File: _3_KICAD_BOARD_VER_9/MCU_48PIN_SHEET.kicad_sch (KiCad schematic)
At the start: 16 parts, among them U2 dsPIC33AK512MPS505T-I/PT, Y1 ABMM-25.000MHZ-B2-T

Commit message: feat : dim only project done
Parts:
- renumbered C18 to C10, C19 to C11, C20 to C12, C21 to C13, C22 to C14, C23 to C15, C24 to C16, C25 to C17, C13 to C5, C14 to C6, C15 to C7, C16 to C8, C17 to C9

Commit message: feat : dim board base board 작업시작
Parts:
- C10, C12, C14, C15, C16, C5, C6, C8: LCSC Part # (none) -> C14663
- C11: LCSC Part # (none) -> C19702
- C13, C17: LCSC Part # (none) -> C107040
- C7: LCSC Part # (none) -> C140782
- C9: LCSC Part # (none) -> C5199872
- L1: LCSC Part # (none) -> C86083
- Y1: LCSC Part # (none) -> C596927
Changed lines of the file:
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@@
+			)
+		)
+		(property "LCSC Part #" "C140782"
+			(at 35.56 41.91 0)
+			(effects
+				(font
+					(size 1.27 1.27)
+				)
+				(hide yes)
 			)
 		)
@@
 			)
 		)
+		(property "LCSC Part #" "C596927"
+			(at 232.41 143.51 0)
+			(effects
+				(font
+					(size 1.27 1.27)
+				)
+				(hide yes)
+			)
+		)
 		(pin "4"
 		)
@@
 			)
 		)
+		(property "LCSC Part #" "C14663"
+			(at 38.1 78.74 0)
+			(effects
+				(font
+					(size 1.27 1.27)
+				)
+				(hide yes)
+			)
+		)
 		(pin "2"
 		)
@@
 			)
 		)
+		(property "LCSC Part #" "C107040"
+			(at 246.38 146.05 0)
+			(effects
+				(font
+					(size 1.27 1.27)
+				)
+				(hide yes)
+			)
+		)
 		(pin "1"
 		)
@@
 			)
 		)
+		(property "LCSC Part #" "C14663"
+			(at 160.02 33.02 0)
+			(effects
+				(font
+					(size 1.27 1.27)
+				)
+				(hide yes)
+			)
+		)
 		(pin "2"
 		)
@@
 			)
 		)
+		(property "LCSC Part #" "C14663"
+			(at 224.79 95.25 0)
+			(effects
+				(font
+					(size 1.27 1.27)
+				)
+				(hide yes)
+			)
+		)
 		(pin "2"
 		)
@@
 			)
 		)
+		(property "LCSC Part #" "C107040"
+			(at 214.63 146.05 0)
+			(effects
+				(font
+					(size 1.27 1.27)
+				)
+				(hide yes)
+			)
+		)
 		(pin "1"
 		)
@@
 			)
 		)
+		(property "LCSC Part #" "C14663"
+			(at 227.33 69.85 0)
+			(effects
+				(font
+					(size 1.27 1.27)
+				)
+				(hide yes)
+			)
+		)
 		(pin "2"
 		)
@@
 			)
 		)
+		(property "LCSC Part #" "C14663"
+			(at 207.01 33.02 0)
+			(effects
+				(font
+					(size 1.27 1.27)
+				)
+				(hide yes)
+			)
+		)
 		(pin "2"
 		)
@@
 			)
 		)
+		(property "LCSC Part #" ""
+			(at 80.01 62.23 0)
+			(effects
+				(font
+					(size 1.27 1.27)
+				)
+				(hide yes)
+			)
+		)
 		(pin "11"
 		)
@@
 			)
 		)
+		(property "LCSC Part #" "C5199872"
+			(at 45.72 41.91 0)
+			(effects
+				(font
+					(size 1.27 1.27)
+				)
+				(hide yes)
+			)
+		)
 		(pin "2"
 		)
@@
 			)
 		)
+		(property "LCSC Part #" "C86083"
+			(at 187.96 30.48 90)
+			(effects
+				(font
+					(size 1.27 1.27)
+				)
+				(hide yes)
+			)
+		)
 		(pin "2"
 		)
@@
 			)
 		)
+		(property "LCSC Part #" "C19702"
+			(at 195.58 33.02 0)
+			(effects
+				(font
+					(size 1.27 1.27)
+				)
+				(hide yes)
+			)
+		)
 		(pin "2"
 		)
@@
 			)
 		)
+		(property "LCSC Part #" "C14663"
+			(at 232.41 115.57 0)
+			(effects
+				(font
+					(size 1.27 1.27)
+				)
+				(hide yes)
+			)
+		)
 		(pin "2"
 		)
@@
 			)
 		)
+		(property "LCSC Part #" "C14663"
+			(at 34.29 100.33 0)
+			(effects
+				(font
+					(size 1.27 1.27)
+				)
+				(hide yes)
+			)
+		)
 		(pin "2"
 		)
@@
 			(at 29.21 113.03 0)
 			(effects
+				(font
+					(size 1.27 1.27)
+				)
+				(hide yes)
+			)
+		)
+		(property "LCSC Part #" "C14663"
+			(at 29.21 113.03 0)
+			(effects

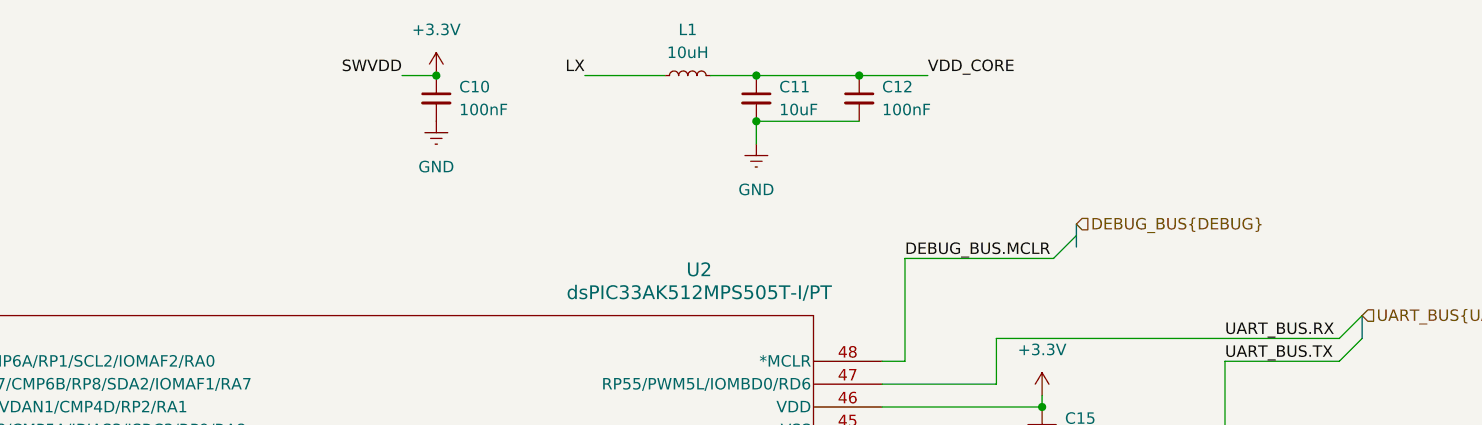
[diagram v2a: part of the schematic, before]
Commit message: feat : 회로도 수정, MCLR pull up 10K 추가, GND MCU쪽 floating 다수...
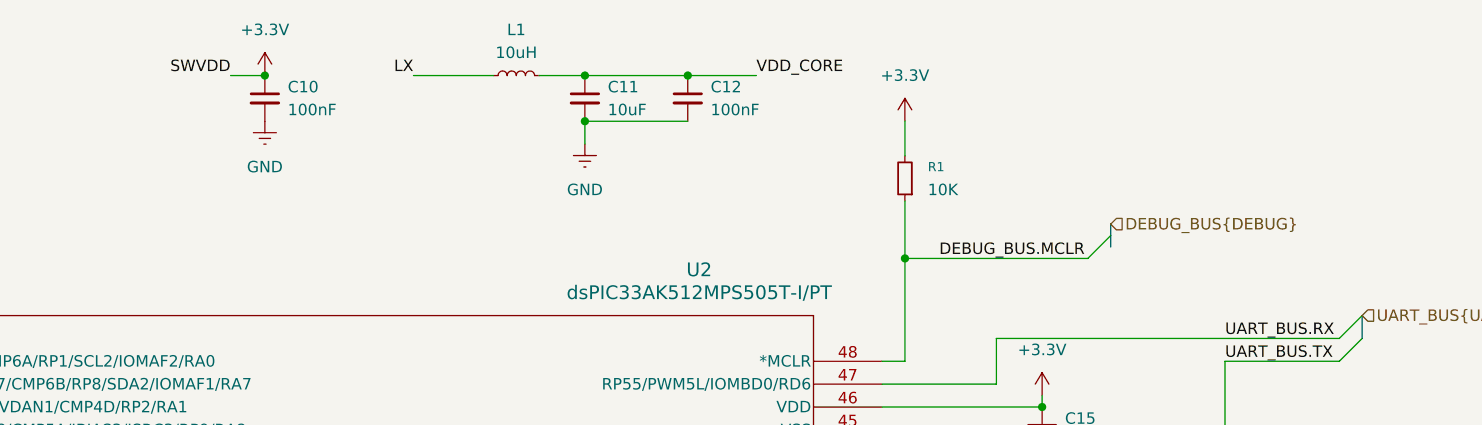
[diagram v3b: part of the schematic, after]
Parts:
- added R1: 10K, Resistor_SMD:R_0603_1608Metric, symbol Device:R_Small
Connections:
- net +3.3V: now also R1.2
- net DEBUG_BUS.MCLR: now also R1.1
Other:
- moved on the sheet: C10, C11, C12, L1

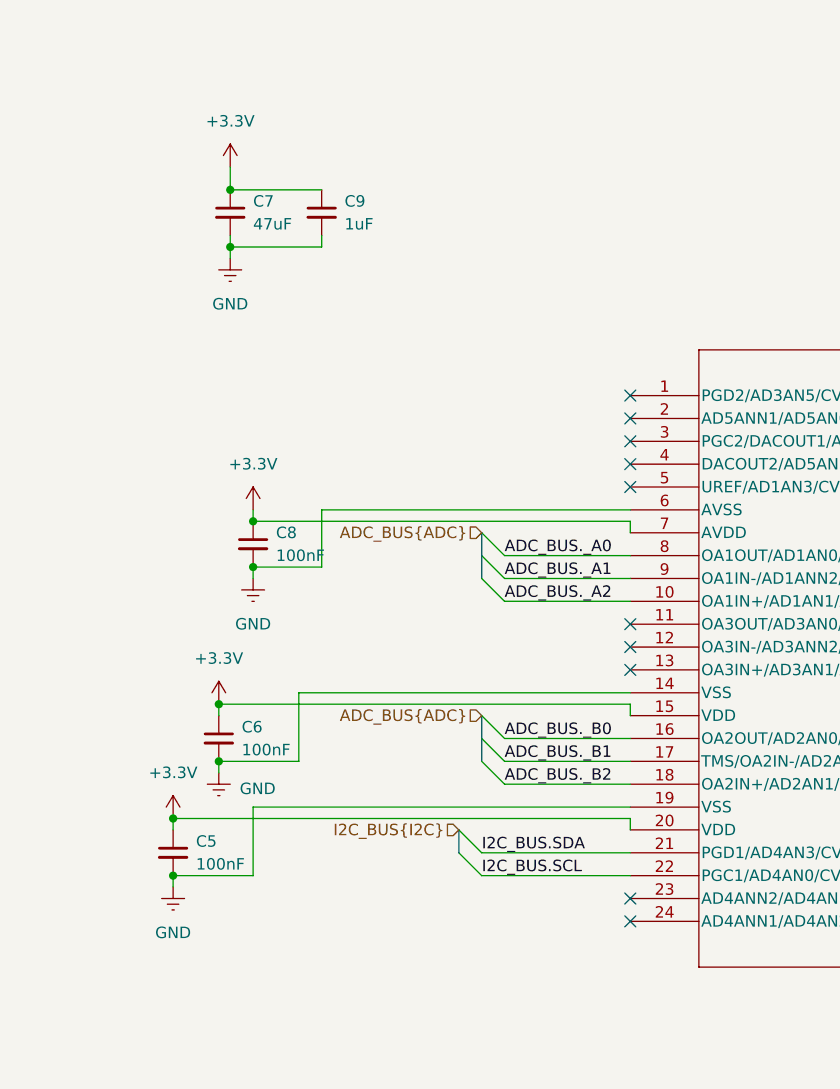
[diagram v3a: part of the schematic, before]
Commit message: feat : 회로도 업데이트
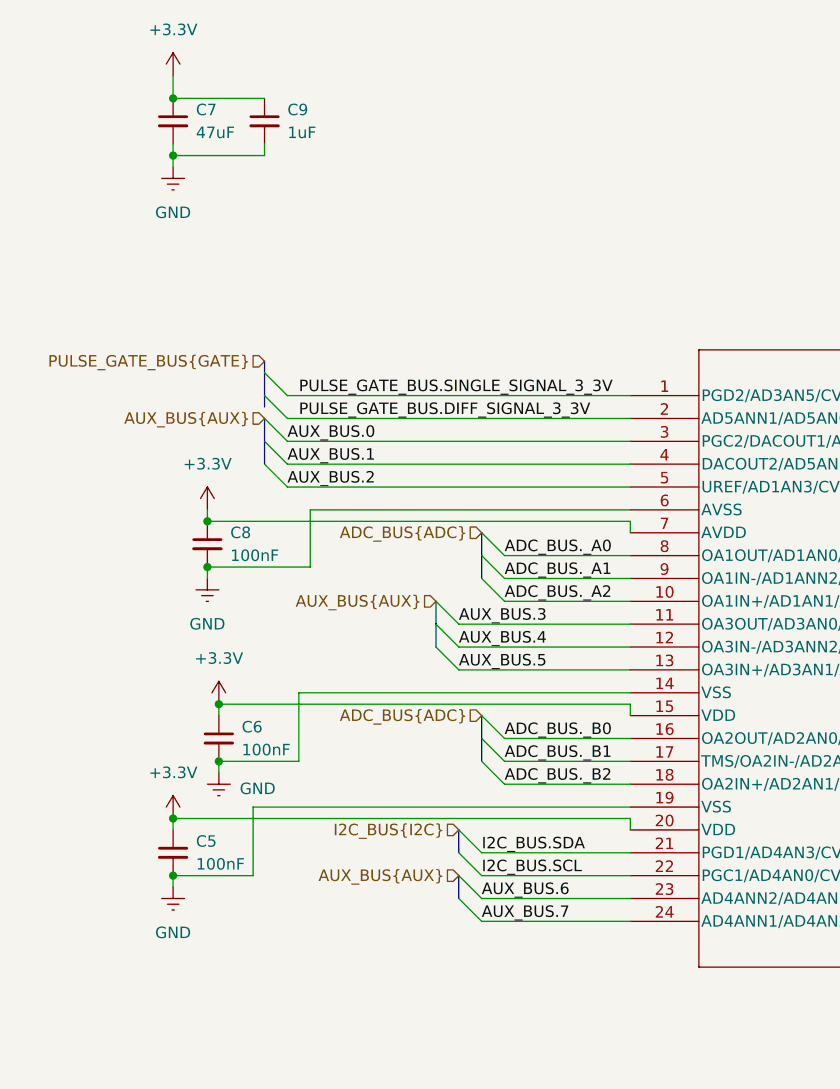
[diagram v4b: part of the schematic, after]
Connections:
- net PULSE_GATE_BUS.SINGLE_SIGNAL_3_3V: now reaches U2.1 (PGD2/AD3AN5/CVDAN0/CMP6A/RP1/SCL2/IOMAF2/RA0)
- net AUX_BUS.3: now reaches U2.11 (OA3OUT/AD3AN0/CVDAN5/CMP3A/RP6/INT0/RA5)
- net AUX_BUS.4: now reaches U2.12 (OA3IN-/AD3ANN2/AD3AN2/CVDAN6/CMPDN/CMP3C/RP7/RA6)
- net AUX_BUS.5: now reaches U2.13 (OA3IN+/AD3AN1/AD4AN5/CVDAN21/CVDTX5/CMP3B/RP22/RB5)
- net PULSE_GATE_BUS.DIFF_SIGNAL_3_3V: now reaches U2.2 (AD5ANN1/AD5AN0/CVDAN7/CMP6B/RP8/SDA2/IOMAF1/RA7)
- net AUX_BUS.6: now reaches U2.23 (AD4ANN2/AD4AN1/CVDAN22/CVDTX6/CMP/CMP7D/IBIAS0/ISRC0/RP23/RB6)
- net AUX_BUS.7: now reaches U2.24 (AD4ANN1/AD4AN2/CVDAN23/CVDTX7/CMP4C/IBIAS1/ISRC1/RP24/IOMAF0/RB7)
- net AUX_BUS.0: now reaches U2.3 (PGC2/DACOUT1/AD5AN1/CVDAN1/CMP4D/RP2/RA1)
- net AUX_BUS.1: now reaches U2.4 (DACOUT2/AD5AN3/CVDAN8/CMP5A/IBIAS3/ISRC3/RP9/RA8)
- net AUX_BUS.2: now reaches U2.5 (UREF/AD1AN3/CVDAN9/CMP5B/CMP7A/IBIAS2/ISRC2/RP10/RA9)
- no-connect marks 12 -> 2
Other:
- moved on the sheet: C7, C8, C9
